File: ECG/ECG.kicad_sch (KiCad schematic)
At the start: 92 parts, among them J1 Conn_01x03, J10 Socket 1x15, J11 Shunt block, J12 Shunt block, J13 Shunt block, J14 Shunt block, J15 Shunt block, J16 Shunt block, J17 Conn_02x04_Odd_Even, J2 Conn_01x03, J3 Conn_02x15_Odd_Even, J4 Conn_02x15_Odd_Even, J5 Conn_01x02, J6 Conn_01x02, J7 Conn_01x03, J8 Conn_02x05_Odd_Even, J9 Socket 1x15, Q1 DMG2301L, Q2 T2N7002AK, Q3 T2N7002AK, Q4 T2N7002AK, Q5 T2N7002AK, Q6 T2N7002AK, U1 AD8232ACPZ-R7, U2 MIC920YC5-TR, U3 ABX00027

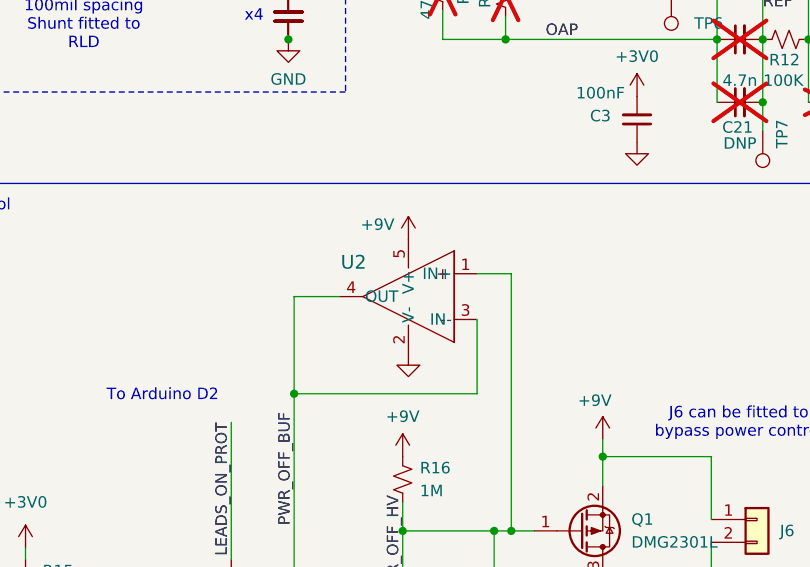
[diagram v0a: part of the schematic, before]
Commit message: Replace high leakage op-amp with slower low power variant to minimize input current requirements.
Close #25
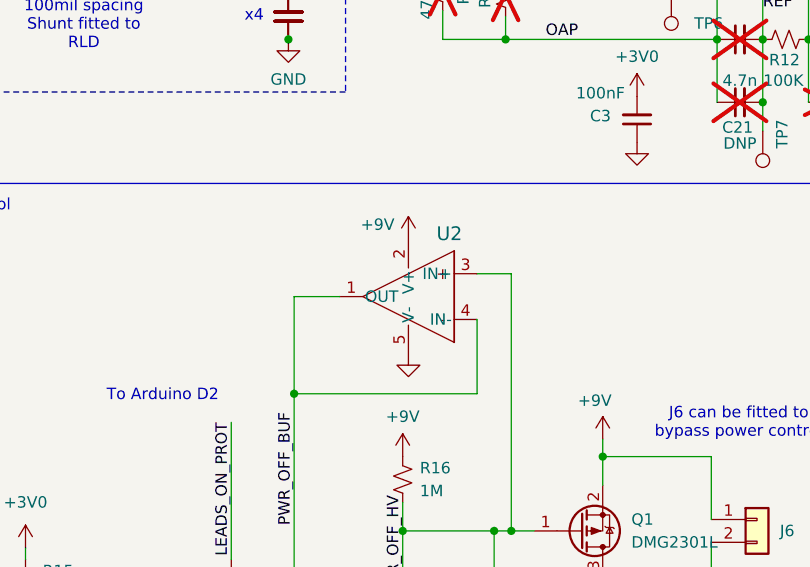
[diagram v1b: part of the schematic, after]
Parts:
- removed U2: MIC920YC5-TR, SC-70_C5_MCH, symbol StockedComponents:MIC920YC5-TR
- added U2: LMC7101BYM5, Package_TO_SOT_SMD:SOT-23-5, symbol StockedComponents:LMC7101BYM5
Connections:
- net +9V: now also U2.2 (V+)
- net GND: now also U2.5 (V-)
- net PWR_OFF_BUF: now also U2.1 (OUT), U2.4 (IN-)
- net PWR_OFF_HV: now also U2.3 (IN+)
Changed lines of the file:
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@@
 	)
 	(symbol
-		(lib_id "StockedComponents:MIC920YC5-TR")
-		(at 86.995 121.285 0)
-		(mirror y)
-		(unit 1)
-		(exclude_from_sim no)
-		(in_bom yes)
-		(on_board yes)
-		(dnp no)
-		(property "Reference" "U2"
-			(at 68.199 120.015 0)
-			(effects
-				(font
-					(size 1.524 1.524)
-				)
-			)
-		)
-		(property "Value" "MIC920YC5-TR"
-			(at 52.705 119.9448 0)
-			(effects
-				(font
-					(size 1.524 1.524)
-				)
-				(hide yes)
-			)
-		)
-		(property "Footprint" "SC-70_C5_MCH"
-			(at 86.995 121.285 0)
-			(effects
-				(font
-					(size 1.27 1.27)
-					(italic yes)
-				)
-				(hide yes)
-			)
-		)
-		(property "Datasheet" "MIC920YC5-TR"
-			(at 86.995 121.285 0)
-			(effects
-				(font
-					(size 1.27 1.27)
-					(italic yes)
-				)
-				(hide yes)
-			)
-		)
-		(property "Description" ""
-			(at 86.995 121.285 0)
-			(effects
-				(font
-					(size 1.27 1.27)
-				)
-				(hide yes)
-			)
-		)
-		(pin "4"
-		)
-		(pin "1"
-		)
-		(pin "2"
-		)
-		(pin "3"
-		)
-		(pin "5"
-		)
-		(instances
-			(project ""
-				(path "/e3a79443-8349-4546-8b4f-331bcc551083"
-					(reference "U2")
-					(unit 1)
-				)
-			)
-		)
-	)
-	(symbol
 		(lib_id "power:GND")
 		(at 269.875 71.755 0)
@@
 					(unit 1)
 				)
+			)
+		)
+	)
+	(symbol
+		(lib_id "StockedComponents:LMC7101BYM5")
+		(at 86.995 121.285 0)
+		(mirror y)
+		(unit 1)
+		(exclude_from_sim no)
+		(in_bom yes)
+		(on_board yes)
+		(dnp no)
+		(fields_autoplaced yes)
+		(property "Reference" "U2"
+			(at 77.4131 116.84 0)
+			(effects
+				(font
+					(size 1.524 1.524)
+				)
+				(justify right)
+			)
+		)
+		(property "Value" "LMC7101BYM5"
+			(at 70.485 120.015 0)
+			(effects
+				(font
+					(size 1.524 1.524)
+				)
+				(hide yes)
+			)
+		)
+		(property "Footprint" "Package_TO_SOT_SMD:SOT-23-5"
+			(at 86.995 121.285 0)
+			(effects
+				(font
+					(size 1.27 1.27)
+					(italic yes)
+				)
+				(hide yes)
+			)
+		)
+		(property "Datasheet" "https://ww1.microchip.com/downloads/en/DeviceDoc/LMC7101-Low-Power-Operational-Amplifier-DS20006282A.pdf"
+			(at 86.995 121.285 0)
+			(effects
+				(font
+					(size 1.27 1.27)
+					(italic yes)
+				)
+				(hide yes)
+			)
+		)
+		(property "Description" "Low Power Slow Op Amp"
+			(at 86.995 121.285 0)
+			(effects
+				(font
+					(size 1.27 1.27)
+				)
+				(hide yes)
+			)
+		)
+		(pin "5"
+		)
+		(pin "1"
+		)
+		(pin "3"
+		)
+		(pin "4"
+		)
+		(pin "2"
+		)
+		(instances
+			(project ""
+				(path "/e3a79443-8349-4546-8b4f-331bcc551083"
+					(reference "U2")
+					(unit 1)
+				)

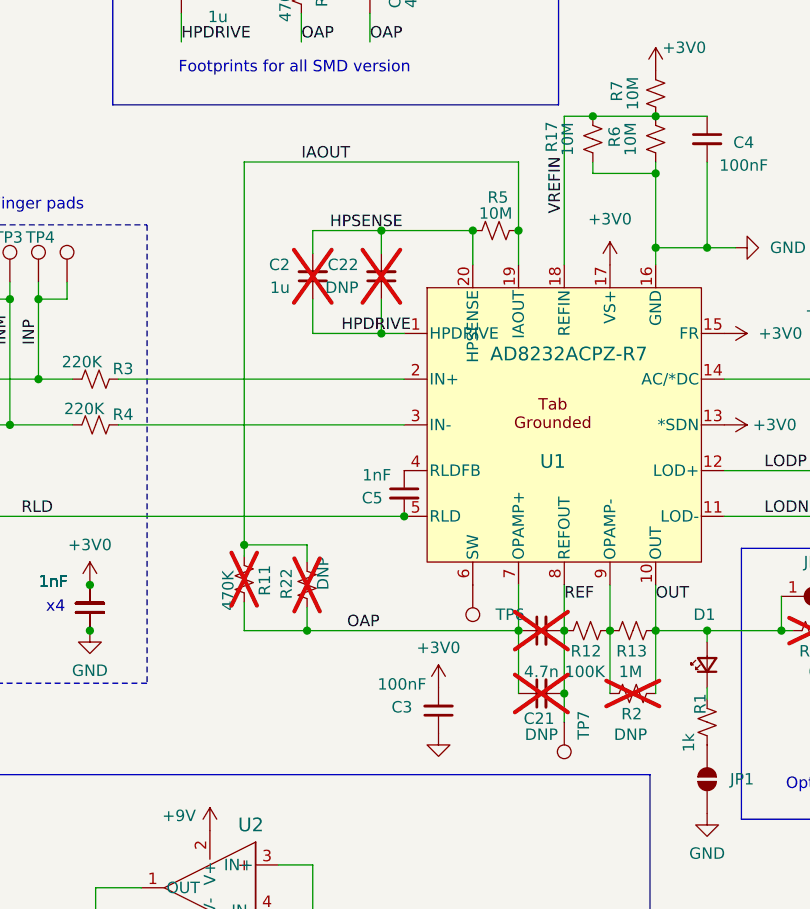
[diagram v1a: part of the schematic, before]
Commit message: remove some redundant(er) THD footprints
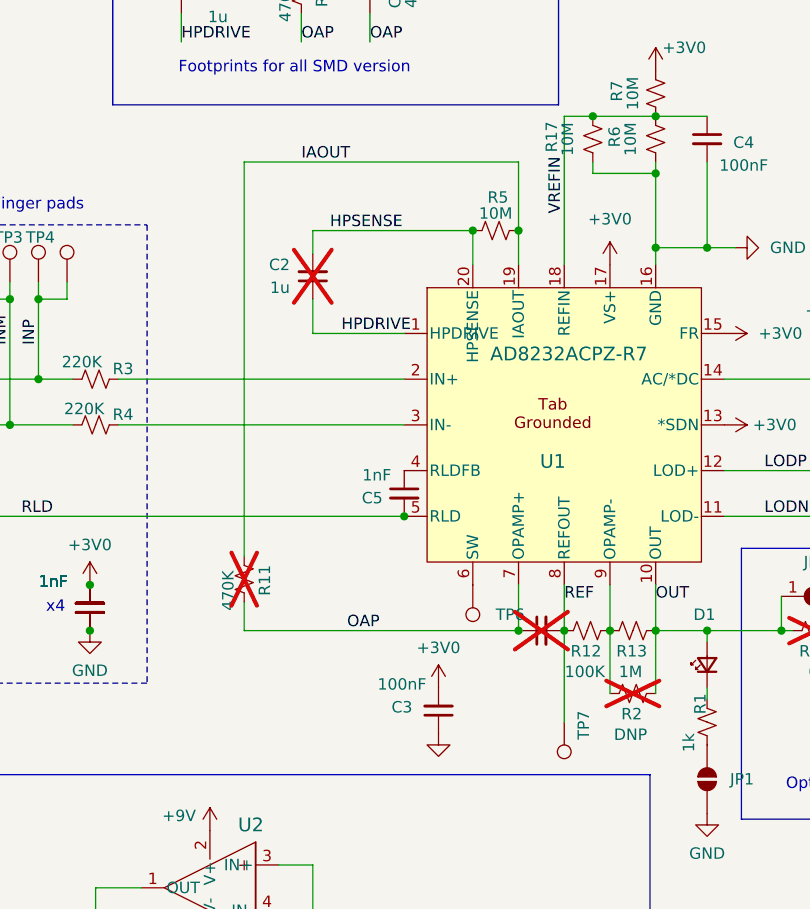
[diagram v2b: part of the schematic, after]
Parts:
- removed C21, C22: DNP, Capacitor_THT:C_Rect_L7.2mm_W5.5mm_P5.00mm_FKS2_FKP2_MKS2_MKP2, symbol Device:C_Small
- removed R22: DNP, Resistor_THT:R_Axial_DIN0207_L6.3mm_D2.5mm_P2.54mm_Vertical, symbol Device:R_Small_US

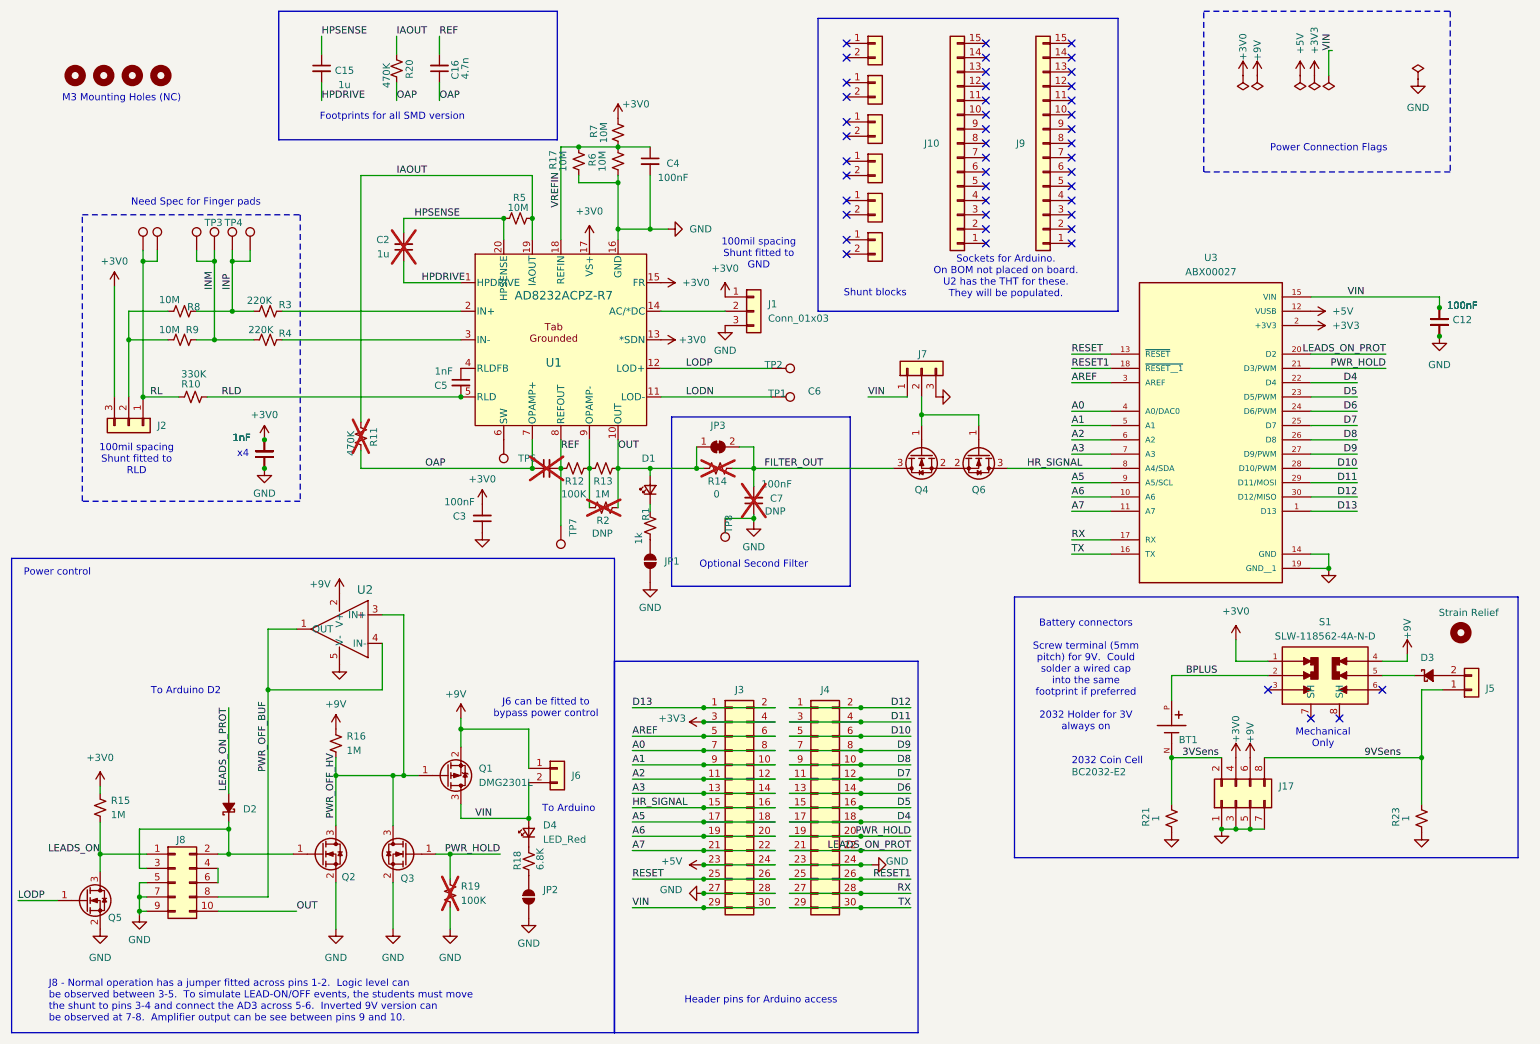
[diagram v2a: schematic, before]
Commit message: add socket for arduino into bom.  exclude arduino from board.
Add decap for new op-amp.

Close #39
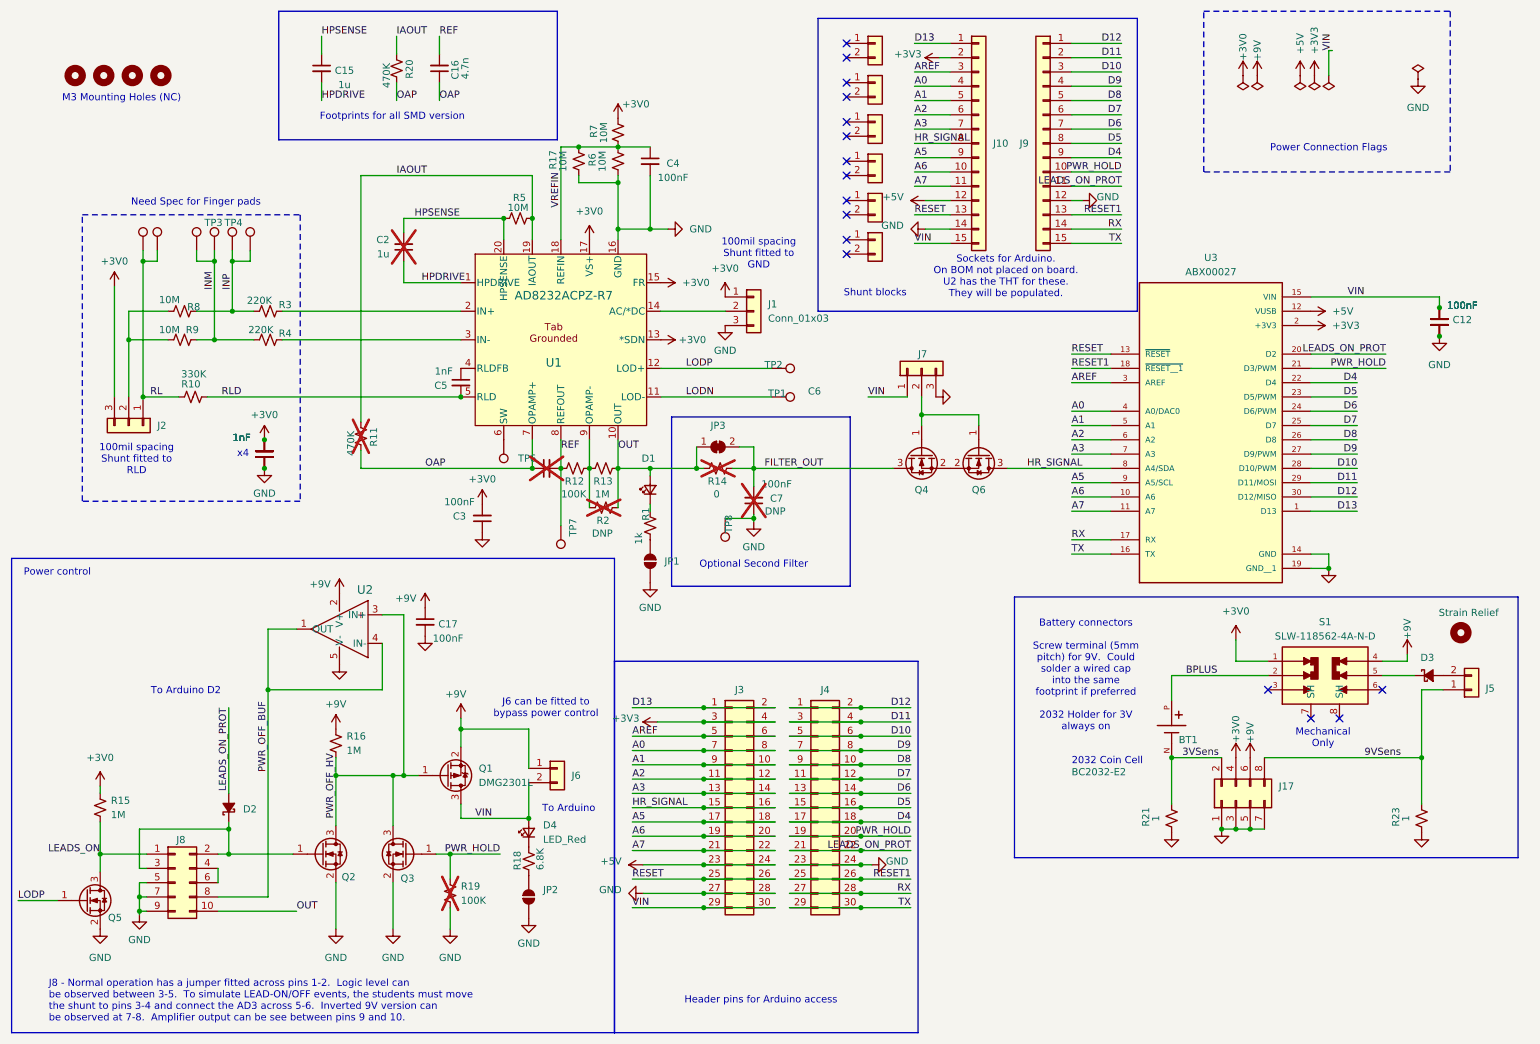
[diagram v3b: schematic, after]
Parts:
- added C17: 100nF, Capacitor_SMD:C_0603_1608Metric, symbol Device:C_Small
- J10, JP3, TP1, TP10, TP11, TP2, TP3, TP4, TP5, TP6, TP7, TP8, TP9: now left out of the parts list
- J9: footprint Connector_PinHeader_2.54mm:PinHeader_1x15_P2.54mm_Vertical -> Connector_PinSocket_2.54mm:PinSocket_1x15_P2.54mm_Vertical; now left out of the parts list
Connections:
- net +3V3: now also J10.2 (Pin_2)
- net +5V: now also J10.12 (Pin_12)
- net +9V: now also C17.1
- net A0: now also J10.4 (Pin_4)
- net A1: now also J10.5 (Pin_5)
- net A2: now also J10.6 (Pin_6)
- net A3: now also J10.7 (Pin_7)
- net A5: now also J10.9 (Pin_9)
- net A6: now also J10.10 (Pin_10)
- net A7: now also J10.11 (Pin_11)
- net AREF: now also J10.3 (Pin_3)
- net D10: now also J9.3 (Pin_3)
- net D11: now also J9.2 (Pin_2)
- net D12: now also J9.1 (Pin_1)
- net D13: now also J10.1 (Pin_1)
- net D4: now also J9.9 (Pin_9)
- net D5: now also J9.8 (Pin_8)
- net D6: now also J9.7 (Pin_7)
- net D7: now also J9.6 (Pin_6)
- net D8: now also J9.5 (Pin_5)
- net D9: now also J9.4 (Pin_4)
- net GND: now also J10.14 (Pin_14), J9.12 (Pin_12), C17.2
- net HR_SIGNAL: now also J10.8 (Pin_8)
- net LEADS_ON_PROT: now also J9.11 (Pin_11)
- net PWR_HOLD: now also J9.10 (Pin_10)
- net RESET: now also J10.13 (Pin_13)
- net RESET1: now also J9.13 (Pin_13)
- net RX: now also J9.14 (Pin_14)
- net TX: now also J9.15 (Pin_15)
- net VIN: now also J10.15 (Pin_15)
- no-connect marks 46 -> 16
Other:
- moved on the sheet: J10

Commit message: part numbers for the pins
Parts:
- D1, D4, U3: now left out of the parts list
- J10, J9: now in the parts list
- J17: DigikeyPN (none) -> 2057-PH2-08-UA-ND
- J3, J4: DigikeyPN (none) -> 732-5306-ND
- U2: DigikeyPN (none) -> 576-2575-1-ND
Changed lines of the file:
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@@
 			)
 		)
+		(property "DigikeyPN" "732-5306-ND"
+			(at 144.145 155.575 0)
+			(effects
+				(font
+					(size 1.27 1.27)
+				)
+				(hide yes)
+			)
+		)
 		(pin "8"
 		)
@@
 		(unit 1)
 		(exclude_from_sim no)
-		(in_bom no)
+		(in_bom yes)
 		(on_board yes)
 		(dnp no)
@@
 			)
 		)
+		(property "DigikeyPN" "2057-PH2-08-UA-ND"
+			(at 233.68 154.305 90)
+			(effects
+				(font
+					(size 1.27 1.27)
+				)
+				(hide yes)
+			)
+		)
 		(pin "1"
 		)
@@
 		(unit 1)
 		(exclude_from_sim no)
-		(in_bom yes)
+		(in_bom no)
 		(on_board yes)
 		(dnp no)
@@
 		(unit 1)
 		(exclude_from_sim no)
-		(in_bom yes)
+		(in_bom no)
 		(on_board no)
 		(dnp no)
@@
 		(unit 1)
 		(exclude_from_sim no)
-		(in_bom yes)
+		(in_bom no)
 		(on_board yes)
 		(dnp no)
@@
 			)
 		)
+		(property "DigikeyPN" "576-2575-1-ND"
+			(at 86.995 121.285 0)
+			(effects
+				(font
+					(size 1.27 1.27)
+				)
+				(hide yes)
+			)
+		)
 		(pin "5"
 		)
@@
 		(unit 1)
 		(exclude_from_sim no)
-		(in_bom no)
+		(in_bom yes)
 		(on_board yes)
 		(dnp no)
@@
 			(at 159.385 155.575 0)
 			(effects
+				(font
+					(size 1.27 1.27)
+				)
+				(hide yes)
+			)
+		)
+		(property "DigikeyPN" "732-5306-ND"
+			(at 159.385 155.575 0)
+			(effects

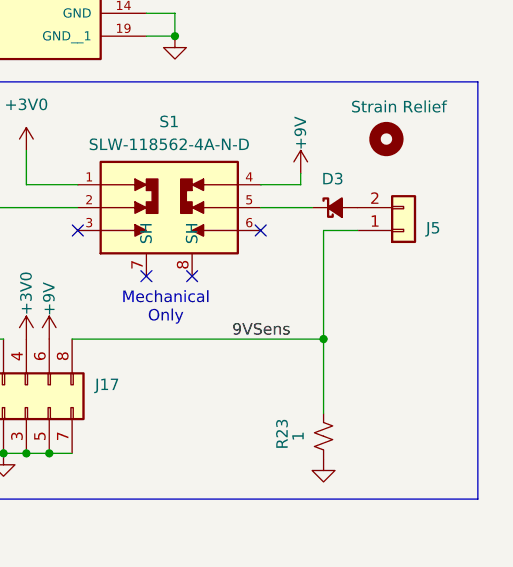
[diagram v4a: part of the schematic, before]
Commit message: add bom only part to hold 9V battery connector
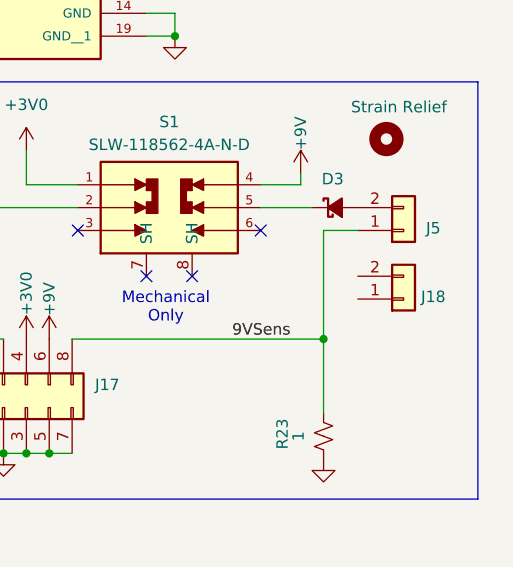
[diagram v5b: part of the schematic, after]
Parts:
- added J18: Conn_01x02, symbol Connector_Generic:Conn_01x02
- J5: AlternatePart 732-10955-ND (TerminalBlock) -> (none); DigikeyPN 36-232-ND -> 732-10955-ND
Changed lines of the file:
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@@
 			)
 		)
-		(property "DigikeyPN" "36-232-ND"
+		(property "DigikeyPN" "732-10955-ND"
 			(at 275.59 134.62 0)
 			(effects
@@
 			)
 		)
-		(property "AlternatePart" "732-10955-ND (TerminalBlock)"
+		(property "AlternatePart" ""
 			(at 275.59 134.62 0)
 			(effects
@@
 					(unit 1)
 				)
+			)
+		)
+	)
+	(symbol
+		(lib_id "Connector_Generic:Conn_01x02")
+		(at 275.59 142.24 0)
+		(mirror x)
+		(unit 1)
+		(exclude_from_sim no)
+		(in_bom yes)
+		(on_board no)
+		(dnp no)
+		(property "Reference" "J18"
+			(at 278.892 141.986 0)
+			(effects
+				(font
+					(size 1.27 1.27)
+				)
+			)
+		)
+		(property "Value" "Conn_01x02"
+			(at 278.13 139.7001 0)
+			(effects
+				(font
+					(size 1.27 1.27)
+				)
+				(justify left)
+				(hide yes)
+			)
+		)
+		(property "Footprint" ""
+			(at 275.59 142.24 0)
+			(effects
+				(font
+					(size 1.27 1.27)
+				)
+				(hide yes)
+			)
+		)
+		(property "Datasheet" ""
+			(at 275.59 142.24 0)
+			(effects
+				(font
+					(size 1.27 1.27)
+				)
+				(hide yes)
+			)
+		)
+		(property "Description" "9V Battery clip"
+			(at 275.59 142.24 0)
+			(effects
+				(font
+					(size 1.27 1.27)
+				)
+				(hide yes)
+			)
+		)
+		(property "DigikeyPN" "36-232-ND"
+			(at 275.59 142.24 0)
+			(effects
+				(font
+					(size 1.27 1.27)
+				)
+				(hide yes)
+			)
+		)
+		(property "Sim.Device" ""
+			(at 275.59 142.24 0)
+			(effects
+				(font
+					(size 1.27 1.27)
+				)
+				(hide yes)
+			)
+		)
+		(property "Sim.Pins" ""
+			(at 275.59 142.24 0)
+			(effects
+				(font
+					(size 1.27 1.27)
+				)
+				(hide yes)
+			)
+		)
+		(property "LCSC" ""
+			(at 275.59 142.24 0)
+			(effects
+				(font
+					(size 1.27 1.27)
+				)
+				(hide yes)
+			)
+		)
+		(property "Manufacturer_PN" ""
+			(at 275.59 142.24 0)
+			(effects
+				(font
+					(size 1.27 1.27)
+				)
+				(hide yes)
+			)
+		)
+		(pin "1"
+		)
+		(pin "2"
+		)
+		(instances
+			(project "ECG"
+				(path "/e3a79443-8349-4546-8b4f-331bcc551083"
+					(reference "J18")
+					(unit 1)
+				)

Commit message: update some part numbers
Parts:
- C1, C12, C13, C14, C17, C3, C4: DigikeyPN 1276-1941-1-ND -> 1276-1000-1-ND
- C15: DigikeyPN 1276-1941-1-ND -> 311-2082-1-ND
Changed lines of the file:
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@@
 			)
 		)
-		(property "DigikeyPN" "1276-1941-1-ND"
+		(property "DigikeyPN" "1276-1000-1-ND"
 			(at 269.875 69.215 0)
 			(effects
@@
 			)
 		)
-		(property "DigikeyPN" "1276-1941-1-ND"
+		(property "DigikeyPN" "1276-1000-1-ND"
 			(at 269.875 69.215 0)
 			(effects
@@
 			)
 		)
-		(property "DigikeyPN" "1276-1941-1-ND"
+		(property "DigikeyPN" "311-2082-1-ND"
 			(at 71.12 24.13 0)
 			(effects
@@
 			)
 		)
-		(property "DigikeyPN" "1276-1941-1-ND"
+		(property "DigikeyPN" "1276-1000-1-ND"
 			(at 99.695 104.14 0)
 			(effects
@@
 			)
 		)
-		(property "DigikeyPN" "1276-1941-1-ND"
+		(property "DigikeyPN" "1276-1000-1-ND"
 			(at 269.875 69.215 0)
 			(effects
@@
 			)
 		)
-		(property "DigikeyPN" "1276-1941-1-ND"
+		(property "DigikeyPN" "1276-1000-1-ND"
 			(at 129.54 40.64 0)
 			(effects
@@
 			)
 		)
-		(property "DigikeyPN" "1276-1941-1-ND"
+		(property "DigikeyPN" "1276-1000-1-ND"
 			(at 269.875 69.215 0)
 			(effects
@@
 			)
 		)
-		(property "DigikeyPN" "1276-1941-1-ND"
+		(property "DigikeyPN" "1276-1000-1-ND"
 			(at 89.535 122.555 0)
 			(effects
